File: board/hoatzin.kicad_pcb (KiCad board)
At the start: 4 copper layers, 221 x 71.5 mm, 60 parts, among them J1 CONN_2-215079-0_TYC, J10 Conn_01x03_Male, J11 Conn_01x03_Male, J12 Conn_01x02_Male, J13 Conn_01x02_Male, J14 Conn_01x03_Male, J15 Conn_01x04_Male, J16 Conn_01x02_Male, J2 CONN_2-215079-0_TYC, J3 671-0501, J4 671-0501, J5 671-0501, J6 292304-1, J7 0702462004, J8 SN37A14B, J9 SN37A14B, U1 STM32L476RGT6, U2 6N139, U3 SN74LS14D, U4 LD3985M33R_SOT23

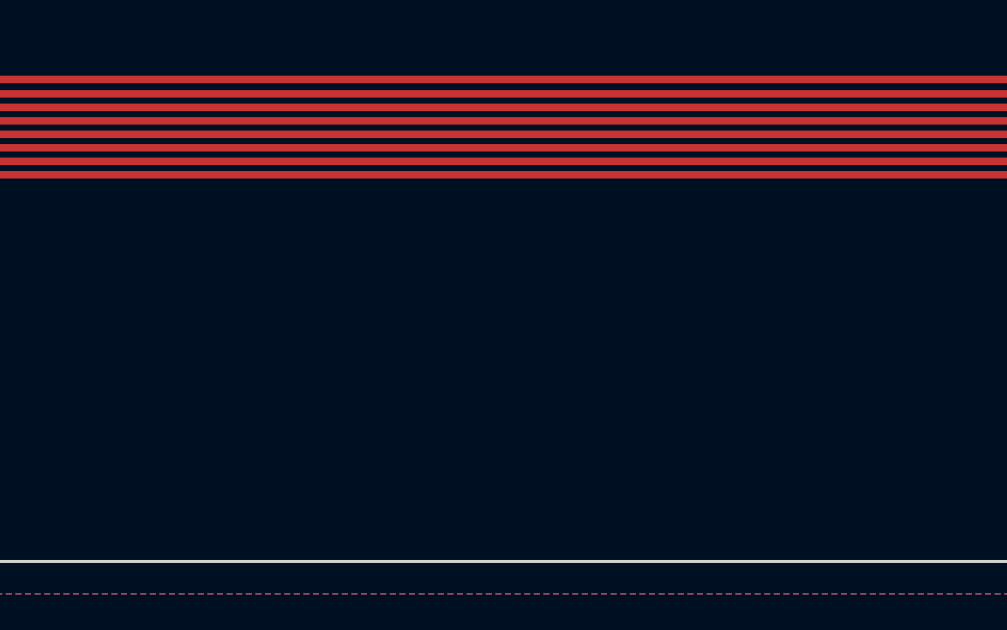
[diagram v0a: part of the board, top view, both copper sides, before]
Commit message: added mizzan silkscreen logo
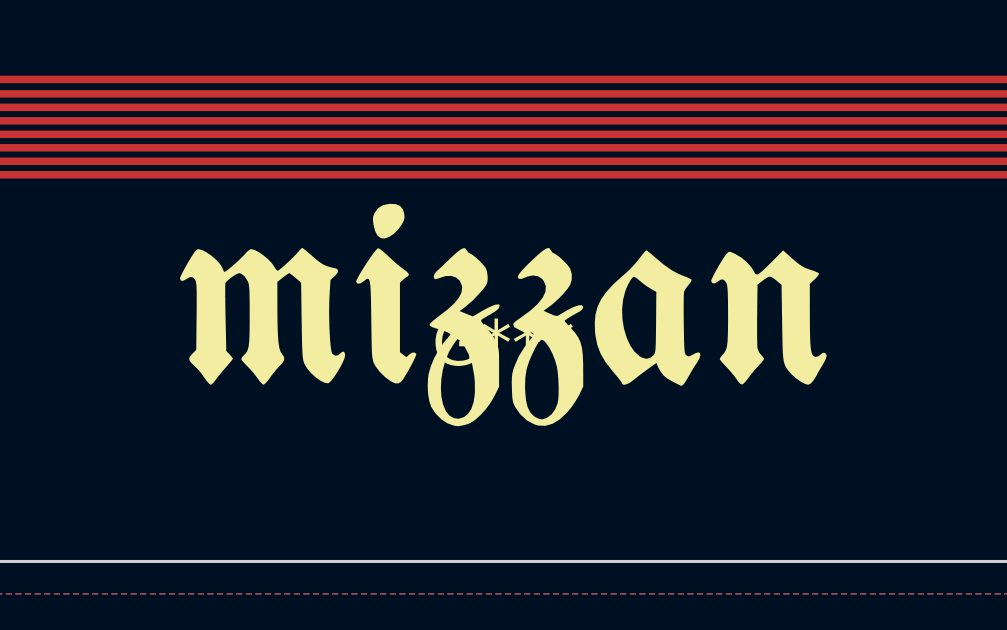
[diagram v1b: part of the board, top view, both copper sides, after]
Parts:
- added G***: LOGO, footprints:mizzan_logo, F.Cu at (100.8, 114.9)
